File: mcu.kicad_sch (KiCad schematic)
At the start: 14 parts, among them J3 DevKit J1, J4 DevKit J3, J5 I2C / Qwiic, J6 WS2812, J7 Rail break-out, U2 74AHCT1G125

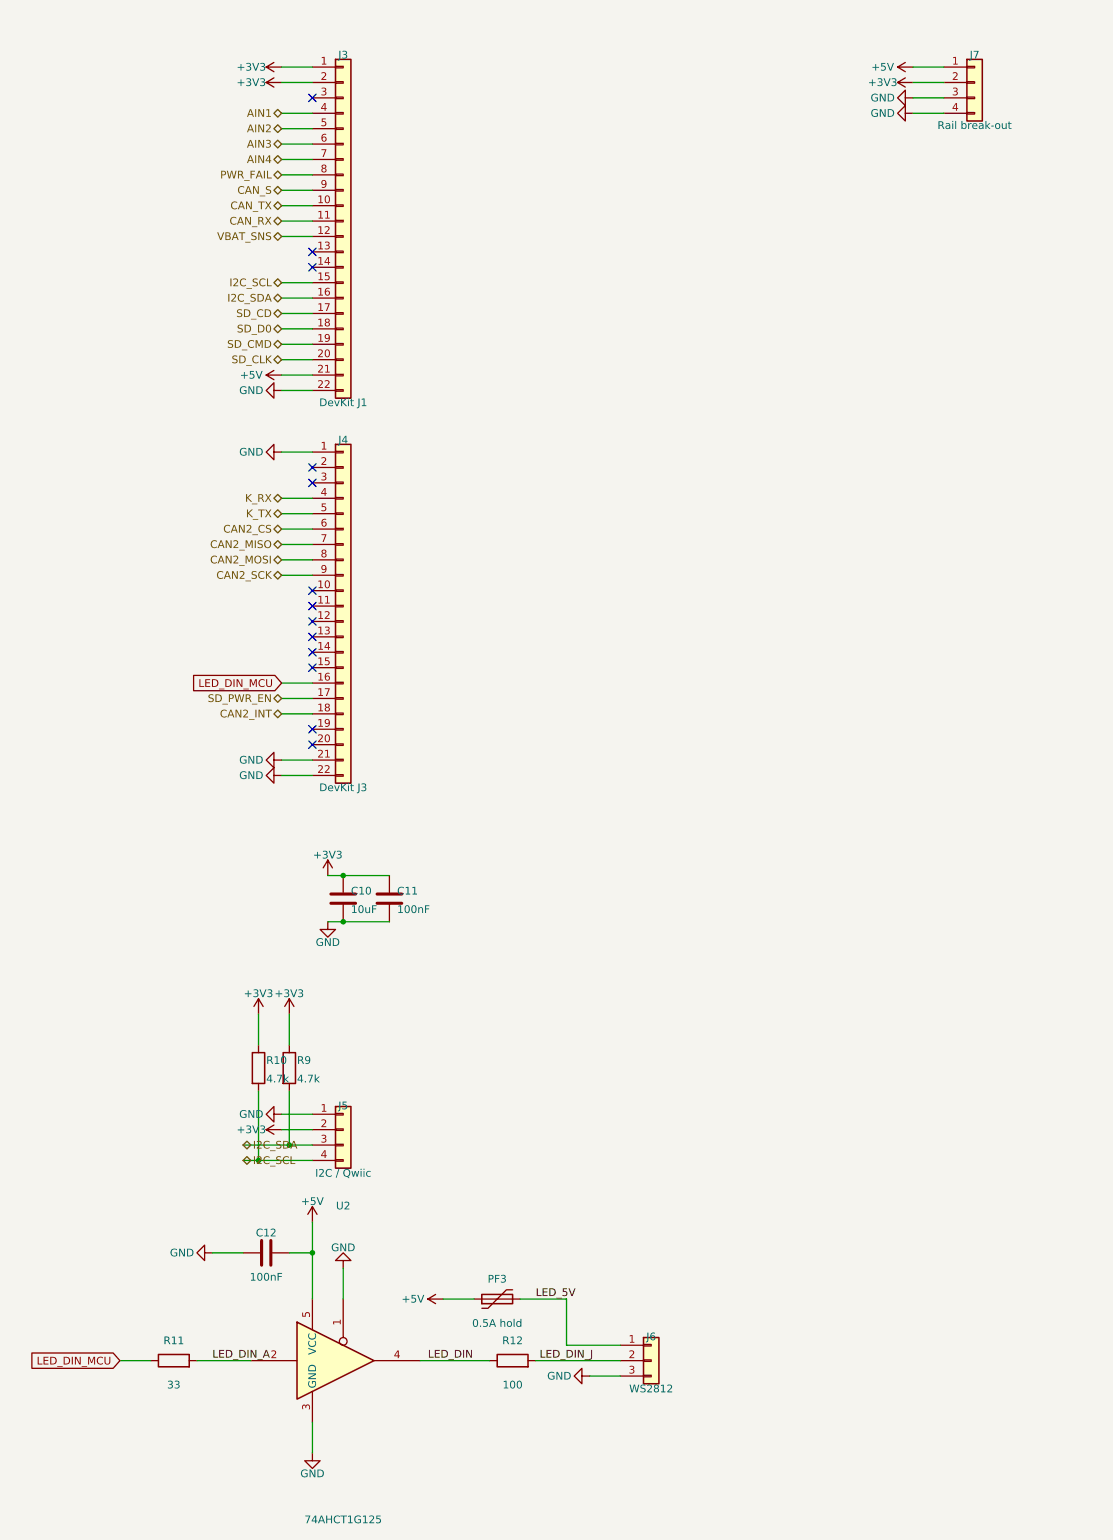
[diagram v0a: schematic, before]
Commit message: Schematic readability: fix the measurement, then fix the schematic
Three bugs in audit_schematic.py meant it was reporting clean on things
that were plainly wrong on the page:

  * lib_info() keyed its table on the NAME_1_1 unit sub-symbols while
    every placed symbol refers to the parent lib_id, so every lookup
    missed, every symbol came back with no pins, and the pin-number
    collisions the function exists to find were never once tested.

  * CHAR_W was an eyeballed 0.70. Plotting the sheets and measuring all
    1141 strings KiCad actually drew gives 0.851. Every string was
    modelled a sixth too narrow -- three characters' worth on a long net
    name.

  * A property's angle is stored RELATIVE to its symbol; KiCad adds the
    symbol's rotation before drawing. Reading the property angle alone
    modelled every field on every rotated part as a tall narrow box
    instead of a long flat one. That is how "SMAJ26CA" and "TERM" came
    to be printed through each other with the audit reporting zero.

Also replaced the "unwired" proxy. It asked whether a wire end lay
within 12 mm of a symbol's ORIGIN, which is fine for an 0603 and wrong
for everything bigger: the MCP2518FD, the microSD socket and both
SRV05-4s were reported floating while fully wired, and the mounting
holes were counted although they have no pins. It now builds the wire
graph and asks whether a symbol shares a conductor with another symbol.

With the measurement honest, the fixing half:

  * gen/tidy_sch_text.py (new), the schematic's tidy_silk.py. Nudges
    colliding references and values, slides a label along its own wire,
    and pulls the free end of a stub outward when a label needs room --
    taking the wire with it so nothing is disconnected. Bodies and
    junctions are obstacles as well as text, because clearing a value
    off a neighbour's value and onto that neighbour's symbol is not a
    fix. Iterates until it stops improving.

  * justify_for(). Block labels hardcoded "just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
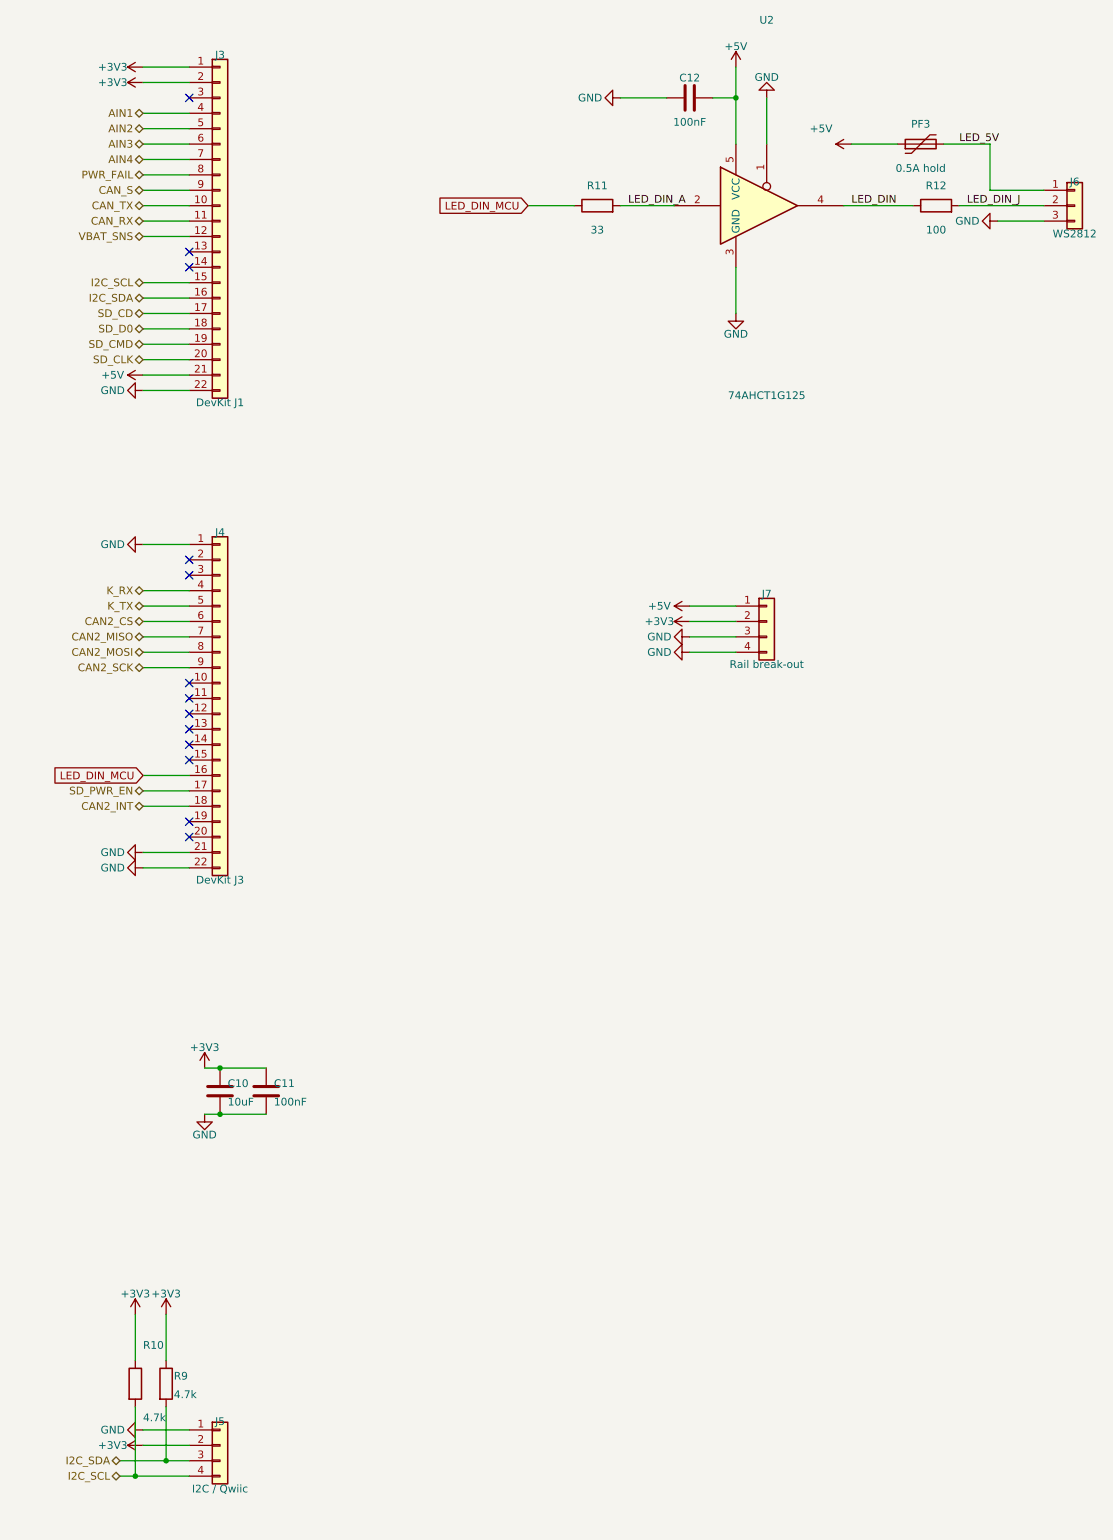
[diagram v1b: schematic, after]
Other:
- moved on the sheet: C10, C11, C12, J3, J4, J5, J6, J7, PF3, R10, R11, R12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
